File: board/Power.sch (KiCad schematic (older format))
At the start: 115 parts, among them CON1 BARREL_JACK, CON2 BARREL_JACK, P1 CONN_2, U12 TPS51200, U4 GBU15005-G, U5 7805_N, U6 TPS54560, U7 TPS53319, U8 TPS54625, U9 TPS54625

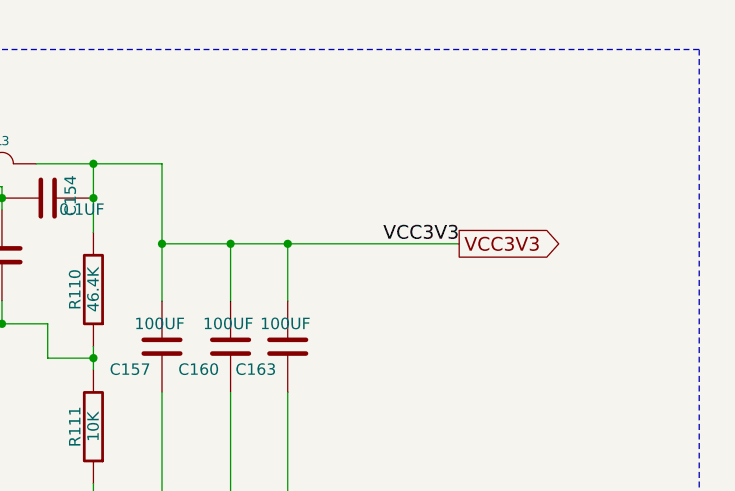
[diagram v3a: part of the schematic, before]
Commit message: Issue #1488 - Added diode display port power pin
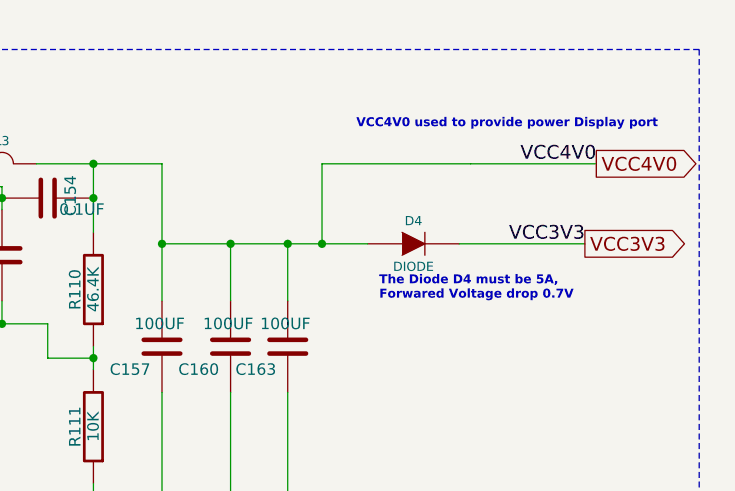
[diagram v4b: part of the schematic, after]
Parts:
- added D4: DIODE, ~, symbol DIODE
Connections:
- net VCC3V3: now also D4.2 (K); no longer C154.1, C157.2, C160.2, C163.2, L3.2, R110.2
- new net VCC4V0: C154.1, C157.2, C160.2, C163.2, D4.1 (A), L3.2, R110.2
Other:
- note added: "The Diode D4 must be 5A, \nForwared Voltage drop 0.7V"
- note added: "VCC4V0 used to provide power Display port"
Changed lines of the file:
@@
 $EndComp
 $Comp
-L GND #PWR01
+L GND #PWR8
 U 1 1 52DD9648
 P 11300 7700
-F 0 "#PWR01" H 11300 7700 30  0001 C CNN
+F 0 "#PWR8" H 11300 7700 30  0001 C CNN
 F 1 "GND" H 11300 7630 30  0001 C CNN
 F 2 "" H 11300 7700 60  0000 C CNN
@@
 $EndComp
 $Comp
-L GND #PWR02
+L GND #PWR12
 U 1 1 52DD9786
 P 12800 5350
-F 0 "#PWR02" H 12800 5350 30  0001 C CNN
+F 0 "#PWR12" H 12800 5350 30  0001 C CNN
 F 1 "GND" H 12800 5280 30  0001 C CNN
 F 2 "" H 12800 5350 60  0000 C CNN
@@
 $EndComp
 $Comp
-L GND #PWR03
+L GND #PWR11
 U 1 1 52DD9A04
 P 11500 1100
-F 0 "#PWR03" H 11500 1100 30  0001 C CNN
+F 0 "#PWR11" H 11500 1100 30  0001 C CNN
 F 1 "GND" H 11500 1030 30  0001 C CNN
 F 2 "" H 11500 1100 60  0000 C CNN
@@
 $EndComp
 $Comp
-L GND #PWR04
+L GND #PWR3
 U 1 1 52DD9A0A
 P 9400 2950
-F 0 "#PWR04" H 9400 2950 30  0001 C CNN
+F 0 "#PWR3" H 9400 2950 30  0001 C CNN
 F 1 "GND" H 9400 2880 30  0001 C CNN
 F 2 "" H 9400 2950 60  0000 C CNN
@@
 	-1   0    0    1
 $EndComp
-Text GLabel 14950 1750 2    60   Output ~ 0
+Text GLabel 15500 1750 2    60   Output ~ 0
 VCC3V3
 Text GLabel 14750 3900 2    60   Output ~ 0
@@
 $EndComp
 $Comp
-L GND #PWR05
+L GND #PWR1
 U 1 1 52E1FEA6
 P 4000 1950
-F 0 "#PWR05" H 4000 1950 30  0001 C CNN
+F 0 "#PWR1" H 4000 1950 30  0001 C CNN
 F 1 "GND" H 4000 1880 30  0001 C CNN
 F 2 "" H 4000 1950 60  0000 C CNN
@@
 $EndComp
 $Comp
-L GND #PWR06
+L GND #PWR7
 U 1 1 52E4CA76
 P 10900 8600
-F 0 "#PWR06" H 10900 8600 30  0001 C CNN
+F 0 "#PWR7" H 10900 8600 30  0001 C CNN
 F 1 "GND" H 10900 8530 30  0001 C CNN
 F 2 "" H 10900 8600 60  0000 C CNN
@@
 $EndComp
 $Comp
-L GND #PWR07
+L GND #PWR4
 U 1 1 52E4CA88
 P 10450 9800
-F 0 "#PWR07" H 10450 9800 30  0001 C CNN
+F 0 "#PWR4" H 10450 9800 30  0001 C CNN
 F 1 "GND" H 10450 9730 30  0001 C CNN
 F 2 "" H 10450 9800 60  0000 C CNN
@@
 $EndComp
 $Comp
-L GND #PWR08
+L GND #PWR16
 U 1 1 52E4CAA0
 P 13800 9800
-F 0 "#PWR08" H 13800 9800 30  0001 C CNN
+F 0 "#PWR16" H 13800 9800 30  0001 C CNN
 F 1 "GND" H 13800 9730 30  0001 C CNN
 F 2 "" H 13800 9800 60  0000 C CNN
@@
 $EndComp
 $Comp
-L GND #PWR09
+L GND #PWR15
 U 1 1 52E4CAAC
 P 13200 9300
-F 0 "#PWR09" H 13200 9300 30  0001 C CNN
+F 0 "#PWR15" H 13200 9300 30  0001 C CNN
 F 1 "GND" H 13200 9230 30  0001 C CNN
 F 2 "" H 13200 9300 60  0000 C CNN
@@
 $EndComp
 $Comp
-L GND #PWR010
+L GND #PWR9
 U 1 1 52E4CAB8
 P 11350 9950
-F 0 "#PWR010" H 11350 9950 30  0001 C CNN
+F 0 "#PWR9" H 11350 9950 30  0001 C CNN
 F 1 "GND" H 11350 9880 30  0001 C CNN
 F 2 "" H 11350 9950 60  0000 C CNN
@@
 VCC3V3
 $Comp
-L GND #PWR011
+L GND #PWR13
 U 1 1 52E4CABF
 P 12800 9700
-F 0 "#PWR011" H 12800 9700 30  0001 C CNN
+F 0 "#PWR13" H 12800 9700 30  0001 C CNN
 F 1 "GND" H 12800 9630 30  0001 C CNN
 F 2 "" H 12800 9700 60  0000 C CNN
@@
 $EndComp
 $Comp
-L GND #PWR012
+L GND #PWR14
 U 1 1 52E4CACB
 P 13100 9950
-F 0 "#PWR012" H 13100 9950 30  0001 C CNN
+F 0 "#PWR14" H 13100 9950 30  0001 C CNN
 F 1 "GND" H 13100 9880 30  0001 C CNN
 F 2 "" H 13100 9950 60  0000 C CNN
@@
 $EndComp
 $Comp
-L GND #PWR013
+L GND #PWR5
 U 1 1 52F26CB0
 P 10650 3700
-F 0 "#PWR013" H 10650 3700 30  0001 C CNN
+F 0 "#PWR5" H 10650 3700 30  0001 C CNN
 F 1 "GND" H 10650 3630 30  0001 C CNN
 F 2 "" H 10650 3700 60  0000 C CNN
@@
 $EndComp
 $Comp
-L GND #PWR014
+L GND #PWR6
 U 1 1 52F2BB58
 P 10900 6200
-F 0 "#PWR014" H 10900 6200 30  0001 C CNN
+F 0 "#PWR6" H 10900 6200 30  0001 C CNN
 F 1 "GND" H 10900 6130 30  0001 C CNN
 F 2 "" H 10900 6200 60  0000 C CNN
@@
 $EndComp
 $Comp
-L GND #PWR015
+L GND #PWR10
 U 1 1 52F2C00C
 P 11450 6150
-F 0 "#PWR015" H 11450 6150 30  0001 C CNN
+F 0 "#PWR10" H 11450 6150 30  0001 C CNN
 F 1 "GND" H 11450 6080 30  0001 C CNN
 F 2 "" H 11450 6150 60  0000 C CNN
@@
 Text Label 6150 5000 2    39   ~ 0
 GND
-Text Label 14950 1750 2    60   ~ 0
+Text Label 15500 1750 2    60   ~ 0
 VCC3V3
 Text Label 9750 4050 0    60   ~ 0
@@
 	13650 2900 13650 2400
 Connection ~ 13350 2900
-Wire Wire Line
-	13650 1750 14950 1750
 Connection ~ 13650 1750
 Wire Wire Line
@@
 Connection ~ 7400 1800
 $Comp
-L GND #PWR016
+L GND #PWR2
 U 1 1 533EEA66
 P 7400 2850
-F 0 "#PWR016" H 7400 2850 30  0001 C CNN
+F 0 "#PWR2" H 7400 2850 30  0001 C CNN
 F 1 "GND" H 7400 2780 30  0001 C CNN
 F 2 "" H 7400 2850 60  0000 C CNN
@@
 	1    0    0    -1
 $EndComp
+$Comp
+L DIODE D4
+U 1 1 551D68AC
+P 14750 1750
+F 0 "D4" H 14750 1850 40  0000 C CNN
+F 1 "DIODE" H 14750 1650 40  0000 C CNN
+F 2 "~" H 14750 1750 60  0000 C CNN
+F 3 "~" H 14750 1750 60  0000 C CNN
+	1    14750 1750
+	1    0    0    -1
+$EndComp
+Wire Wire Line
+	14950 1750 15500 1750
+Wire Wire Line
+	13650 1750 14550 1750
+Wire Wire Line
+	14350 1750 14350 1400
+Wire Wire Line
+	14350 1400 15000 1400
+Connection ~ 14350 1750
+Text GLabel 15550 1400 2    60   Output ~ 0
+VCC4V0
+Text Label 15550 1400 2    60   ~ 0
+VCC4V0
+Wire Wire Line
+	15000 1400 15550 1400
+Text Notes 14500 1250 0    39   ~ 8
+VCC4V0 used to provide power Display port
+Text Notes 14600 2000 0    39   ~ 8
+The Diode D4 must be 5A, \nForwared Voltage drop 0.7V
 $EndSCHEMATC

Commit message: Issue #1585
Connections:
- net VTTREF: now reaches C153.2, U12.6 (REFOUT)
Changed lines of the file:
@@
 LIBS:contrib
 LIBS:valves
-LIBS:hdmi2usb
-LIBS:timvideos-pcie-8x
 LIBS:HDMI2USB-cache
 EELAYER 27 0
@@
 Sheet 2 12
 Title "HDMI2USB"
-Date "30 mar 2015"
+Date "1 apr 2015"
 Rev "Rev2"
 Comp ""
@@
 $EndComp
 $Comp
-L GND #PWR8
+L GND #PWR01
 U 1 1 52DD9648
 P 11300 7700
-F 0 "#PWR8" H 11300 7700 30  0001 C CNN
+F 0 "#PWR01" H 11300 7700 30  0001 C CNN
 F 1 "GND" H 11300 7630 30  0001 C CNN
 F 2 "" H 11300 7700 60  0000 C CNN
@@
 $EndComp
 $Comp
-L GND #PWR12
+L GND #PWR02
 U 1 1 52DD9786
 P 12800 5350
-F 0 "#PWR12" H 12800 5350 30  0001 C CNN
+F 0 "#PWR02" H 12800 5350 30  0001 C CNN
 F 1 "GND" H 12800 5280 30  0001 C CNN
 F 2 "" H 12800 5350 60  0000 C CNN
@@
 $EndComp
 $Comp
-L GND #PWR11
+L GND #PWR03
 U 1 1 52DD9A04
 P 11500 1100
-F 0 "#PWR11" H 11500 1100 30  0001 C CNN
+F 0 "#PWR03" H 11500 1100 30  0001 C CNN
 F 1 "GND" H 11500 1030 30  0001 C CNN
 F 2 "" H 11500 1100 60  0000 C CNN
@@
 $EndComp
 $Comp
-L GND #PWR3
+L GND #PWR04
 U 1 1 52DD9A0A
 P 9400 2950
-F 0 "#PWR3" H 9400 2950 30  0001 C CNN
+F 0 "#PWR04" H 9400 2950 30  0001 C CNN
 F 1 "GND" H 9400 2880 30  0001 C CNN
 F 2 "" H 9400 2950 60  0000 C CNN
@@
 $EndComp
 $Comp
-L GND #PWR1
+L GND #PWR05
 U 1 1 52E1FEA6
 P 4000 1950
-F 0 "#PWR1" H 4000 1950 30  0001 C CNN
+F 0 "#PWR05" H 4000 1950 30  0001 C CNN
 F 1 "GND" H 4000 1880 30  0001 C CNN
 F 2 "" H 4000 1950 60  0000 C CNN
@@
 $EndComp
 $Comp
-L GND #PWR7
+L GND #PWR06
 U 1 1 52E4CA76
 P 10900 8600
-F 0 "#PWR7" H 10900 8600 30  0001 C CNN
+F 0 "#PWR06" H 10900 8600 30  0001 C CNN
 F 1 "GND" H 10900 8530 30  0001 C CNN
 F 2 "" H 10900 8600 60  0000 C CNN
@@
 $EndComp
 $Comp
-L GND #PWR4
+L GND #PWR07
 U 1 1 52E4CA88
 P 10450 9800
-F 0 "#PWR4" H 10450 9800 30  0001 C CNN
+F 0 "#PWR07" H 10450 9800 30  0001 C CNN
 F 1 "GND" H 10450 9730 30  0001 C CNN
 F 2 "" H 10450 9800 60  0000 C CNN
@@
 $EndComp
 $Comp
-L GND #PWR16
+L GND #PWR08
 U 1 1 52E4CAA0
 P 13800 9800
-F 0 "#PWR16" H 13800 9800 30  0001 C CNN
+F 0 "#PWR08" H 13800 9800 30  0001 C CNN
 F 1 "GND" H 13800 9730 30  0001 C CNN
 F 2 "" H 13800 9800 60  0000 C CNN
@@
 $EndComp
 $Comp
-L GND #PWR15
+L GND #PWR09
 U 1 1 52E4CAAC
 P 13200 9300
-F 0 "#PWR15" H 13200 9300 30  0001 C CNN
+F 0 "#PWR09" H 13200 9300 30  0001 C CNN
 F 1 "GND" H 13200 9230 30  0001 C CNN
 F 2 "" H 13200 9300 60  0000 C CNN
@@
 $EndComp
 $Comp
-L GND #PWR9
+L GND #PWR010
 U 1 1 52E4CAB8
 P 11350 9950
-F 0 "#PWR9" H 11350 9950 30  0001 C CNN
+F 0 "#PWR010" H 11350 9950 30  0001 C CNN
 F 1 "GND" H 11350 9880 30  0001 C CNN
 F 2 "" H 11350 9950 60  0000 C CNN
@@
 VCC3V3
 $Comp
-L GND #PWR13
+L GND #PWR011
 U 1 1 52E4CABF
 P 12800 9700
-F 0 "#PWR13" H 12800 9700 30  0001 C CNN
+F 0 "#PWR011" H 12800 9700 30  0001 C CNN
 F 1 "GND" H 12800 9630 30  0001 C CNN
 F 2 "" H 12800 9700 60  0000 C CNN
@@
 $EndComp
 $Comp
-L GND #PWR14
+L GND #PWR012
 U 1 1 52E4CACB
 P 13100 9950
-F 0 "#PWR14" H 13100 9950 30  0001 C CNN
+F 0 "#PWR012" H 13100 9950 30  0001 C CNN
 F 1 "GND" H 13100 9880 30  0001 C CNN
 F 2 "" H 13100 9950 60  0000 C CNN
@@
 $EndComp
 $Comp
-L GND #PWR5
+L GND #PWR013
 U 1 1 52F26CB0
 P 10650 3700
-F 0 "#PWR5" H 10650 3700 30  0001 C CNN
+F 0 "#PWR013" H 10650 3700 30  0001 C CNN
 F 1 "GND" H 10650 3630 30  0001 C CNN
 F 2 "" H 10650 3700 60  0000 C CNN
@@
 $EndComp
 $Comp
-L GND #PWR6
+L GND #PWR014
 U 1 1 52F2BB58
 P 10900 6200
-F 0 "#PWR6" H 10900 6200 30  0001 C CNN
+F 0 "#PWR014" H 10900 6200 30  0001 C CNN
 F 1 "GND" H 10900 6130 30  0001 C CNN
 F 2 "" H 10900 6200 60  0000 C CNN
@@
 $EndComp
 $Comp
-L GND #PWR10
+L GND #PWR015
 U 1 1 52F2C00C
 P 11450 6150
-F 0 "#PWR10" H 11450 6150 30  0001 C CNN
+F 0 "#PWR015" H 11450 6150 30  0001 C CNN
 F 1 "GND" H 11450 6080 30  0001 C CNN
 F 2 "" H 11450 6150 60  0000 C CNN
@@
 Connection ~ 12800 9650
 Wire Wire Line
-	13100 9500 13100 9450
+	13100 8800 13100 9500
 Wire Wire Line
 	13100 9950 13100 9900
@@
 	5550 5650 5550 5700
 Connection ~ 5550 5700
-Connection ~ 14700 9100
 Wire Wire Line
 	12550 6250 14850 6250
@@
 Connection ~ 7400 1800
 $Comp
-L GND #PWR2
+L GND #PWR016
 U 1 1 533EEA66
 P 7400 2850
-F 0 "#PWR2" H 7400 2850 30  0001 C CNN
+F 0 "#PWR016" H 7400 2850 30  0001 C CNN
 F 1 "GND" H 7400 2780 30  0001 C CNN
 F 2 "" H 7400 2850 60  0000 C CNN
@@
 	14350 1750 14350 1400
 Wire Wire Line
-	14350 1400 15000 1400
+	14350 1400 15550 1400
 Connection ~ 14350 1750
 Text GLabel 15550 1400 2    60   Output ~ 0
@@
 Text Label 15550 1400 2    60   ~ 0
 VCC4V0
-Wire Wire Line
-	15000 1400 15550 1400
 Text Notes 14500 1250 0    39   ~ 8
 VCC4V0 used to provide power Display port
 Text Notes 14600 2000 0    39   ~ 8
 The Diode D4 must be 5A, \nForwared Voltage drop 0.7V
+Wire Wire Line
+	13100 8800 14850 8800
+Connection ~ 13100 9450
+Text GLabel 14850 8800 2    60   Output ~ 0
+VTTREF
 $EndSCHEMATC

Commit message: Issue #1647 - Final changes
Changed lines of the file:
@@
 LIBS:contrib
 LIBS:valves
+LIBS:hdmi2usb
+LIBS:timvideos-pcie-8x
 LIBS:HDMI2USB-cache
 EELAYER 27 0
@@
 Sheet 2 12
 Title "HDMI2USB"
-Date "1 apr 2015"
+Date "2 apr 2015"
 Rev "Rev2"
 Comp ""
@@
 Text GLabel 14850 8800 2    60   Output ~ 0
 VTTREF
+Text Label 14550 6250 0    39   ~ 0
+VCC1V2
 $EndSCHEMATC

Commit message: Issue #1713
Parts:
- removed C46, C49, C50: 47uF, symbol C
- removed C47: 4.7uF, symbol C
- removed U5: 7805_N, ~, symbol 7805_N
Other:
- note removed: "VCC5V0"
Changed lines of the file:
@@
 Sheet 2 12
 Title "HDMI2USB"
-Date "2 apr 2015"
+Date "7 apr 2015"
 Rev "Rev2"
 Comp ""
@@
 Text Label 14750 3900 2    59   ~ 0
 VCC1V5
-Text Notes 1050 7700 0    79   ~ 16
-VCC5V0
-Wire Notes Line
-	900  7750 6750 7750
-Wire Notes Line
-	6750 7750 6750 9650
-Wire Notes Line
-	6750 9650 900  9650
-Wire Notes Line
-	900  9650 900  7750
-Text GLabel 4350 8450 2    60   Output ~ 0
-VCC5V0
-Text Label 3150 8900 2    39   ~ 0
-GND
-Wire Wire Line
-	3250 8900 3250 8750
-Wire Wire Line
-	2450 8900 4250 8900
-$Comp
-L C C47
-U 1 1 54996452
-P 2750 8700
-F 0 "C47" H 2800 8800 50  0000 L CNN
-F 1 "4.7uF" H 2750 8600 50  0000 L CNN
-F 2 "" H 2750 8700 60  0000 C CNN
-F 3 "" H 2750 8700 60  0000 C CNN
-	1    2750 8700
-	-1   0    0    1
-$EndComp
-$Comp
-L C C49
-U 1 1 54996464
-P 3850 8650
-F 0 "C49" H 3900 8750 50  0000 L CNN
-F 1 "47uF" H 3850 8550 50  0000 L CNN
-F 2 "" H 3850 8650 60  0000 C CNN
-F 3 "" H 3850 8650 60  0000 C CNN
-	1    3850 8650
-	-1   0    0    1
-$EndComp
-$Comp
-L C C50
-U 1 1 5499646A
-P 4250 8650
-F 0 "C50" H 4300 8750 50  0000 L CNN
-F 1 "47uF" H 4250 8550 50  0000 L CNN
-F 2 "" H 4250 8650 60  0000 C CNN
-F 3 "" H 4250 8650 60  0000 C CNN
-	1    4250 8650
-	-1   0    0    1
-$EndComp
-$Comp
-L C C46
-U 1 1 54996470
-P 2450 8700
-F 0 "C46" H 2500 8800 50  0000 L CNN
-F 1 "47uF" H 2450 8600 50  0000 L CNN
-F 2 "" H 2450 8700 60  0000 C CNN
-F 3 "" H 2450 8700 60  0000 C CNN
-	1    2450 8700
-	-1   0    0    1
-$EndComp
-Wire Wire Line
-	2850 8450 2450 8450
-Wire Wire Line
-	2450 8450 2450 8500
-Wire Wire Line
-	2750 8500 2750 8450
-Connection ~ 2750 8450
-Connection ~ 2750 8900
-Wire Wire Line
-	3650 8450 4350 8450
-Connection ~ 3850 8450
-Wire Wire Line
-	3850 8900 3850 8850
-Connection ~ 3250 8900
-Wire Wire Line
-	4250 8900 4250 8850
-Connection ~ 3850 8900
-Connection ~ 4250 8450
-$Comp
-L 7805_N U5
-U 1 1 54F86042
-P 3250 8500
-F 0 "U5" H 3400 8304 60  0000 C CNN
-F 1 "7805_N" H 3250 8700 60  0000 C CNN
-F 2 "~" H 3250 8500 60  0000 C CNN
-F 3 "~" H 3250 8500 60  0000 C CNN
-	1    3250 8500
-	1    0    0    -1
-$EndComp
 $Comp
 L DIODE D4
@@
 Text Label 14550 6250 0    39   ~ 0
 VCC1V2
+$Comp
+L PWR_FLAG #FLG017
+U 1 1 55225306
+P 10000 6400
+F 0 "#FLG017" H 10000 6495 30  0001 C CNN
+F 1 "PWR_FLAG" H 10000 6580 30  0000 C CNN
+F 2 "" H 10000 6400 60  0000 C CNN
+F 3 "" H 10000 6400 60  0000 C CNN
+	1    10000 6400
+	1    0    0    -1
+$EndComp
 $EndSCHEMATC
